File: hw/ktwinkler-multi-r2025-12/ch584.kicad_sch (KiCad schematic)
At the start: 13 parts, among them J10 Conn_01x06, J17 Conn_01x02, J18 Conn_01x02, J3 Conn_01x05, U8 CH584F, Y4 32k, Y5 32M

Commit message: hw: save before kicad 10 upgrade
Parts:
- removed J3: Conn_01x05, Connector_PinHeader_2.54mm:PinHeader_1x05_P2.54mm_Vertical, symbol Connector_Generic:Conn_01x05
- added J19: Conn_01x06, Connector_PinHeader_2.54mm:PinHeader_1x06_P2.54mm_Vertical, symbol Connector_Generic:Conn_01x06
- J10: now left out of the parts list
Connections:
- net GND: now also J19.1 (Pin_1), J19.2 (Pin_2)
- net TCK: now also J19.5 (Pin_5)
- net TIO: now also J19.6 (Pin_6)
- net at U8.27 (PA5_TXD3_AIN1): now also J19.4 (Pin_4)
- net at U8.26 (PA4_RXD3_AIN0): now also J19.3 (Pin_3)
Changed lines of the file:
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@@
 	)
 	(junction
+		(at 198.12 104.14)
+		(diameter 0)
+		(color 0 0 0 0)
+	)
+	(junction
 		(at 106.68 60.96)
 		(diameter 0)
@@
 	(wire
 		(pts
-			(xy 198.12 104.14) (xy 200.66 104.14)
-		)
-		(stroke
-			(width 0)
-			(type default)
-		)
-	)
-	(wire
-		(pts
 			(xy 187.96 114.3) (xy 187.96 109.22)
 		)
@@
 	(wire
 		(pts
+			(xy 200.66 101.6) (xy 198.12 101.6)
+		)
+		(stroke
+			(width 0)
+			(type default)
+		)
+	)
+	(wire
+		(pts
 			(xy 96.52 35.56) (xy 96.52 43.18)
 		)
@@
 	(wire
 		(pts
+			(xy 198.12 101.6) (xy 198.12 104.14)
+		)
+		(stroke
+			(width 0)
+			(type default)
+		)
+	)
+	(wire
+		(pts
 			(xy 119.38 40.64) (xy 119.38 38.1)
 		)
@@
 	(wire
 		(pts
+			(xy 198.12 104.14) (xy 200.66 104.14)
+		)
+		(stroke
+			(width 0)
+			(type default)
+		)
+	)
+	(wire
+		(pts
 			(xy 33.02 101.6) (xy 38.1 101.6)
 		)
@@
 		)
 	)
-	(symbol
-		(lib_id "Connector_Generic:Conn_01x02")
-		(at 83.82 109.22 0)
-		(mirror y)
-		(unit 1)
-		(exclude_from_sim no)
-		(in_bom yes)
-		(on_board yes)
-		(dnp no)
-		(property "Reference" "J17"
-			(at 82.5499 106.68 90)
-			(effects
-				(font
-					(size 1.27 1.27)
-				)
-				(justify left)
+	(netclass_flag ""
+		(length 2.54)
+		(shape round)
+		(at 180.34 38.1 0)
+		(fields_autoplaced yes)
+		(effects
+			(font
+				(size 1.27 1.27)
 			)
+			(justify left bottom)
 		)
-		(property "Value" "Conn_01x02"
-			(at 85.0899 106.68 90)
+		(property "Netclass" "k50r"
+			(at 181.0385 35.56 0)
 			(effects
 				(font
@@
 			)
 		)
-		(property "Footprint" "TestPoint:TestPoint_2Pads_Pitch2.54mm_Drill0.8mm"
-			(at 83.82 109.22 0)
+		(property "Component Class" ""
+			(at -93.98 30.48 0)
 			(effects
 				(font
 					(size 1.27 1.27)
+					(italic yes)
 				)
-				(hide yes)
 			)
 		)
-		(property "Datasheet" "~"
-			(at 83.82 109.22 0)
+	)
+	(netclass_flag ""
+		(length 2.54)
+		(shape round)
+		(at 165.1 38.1 0)
+		(fields_autoplaced yes)
+		(effects
+			(font
+				(size 1.27 1.27)
+			)
+			(justify left bottom)
+		)
+		(property "Netclass" "k50r"
+			(at 165.7985 35.56 0)
 			(effects
 				(font
 					(size 1.27 1.27)
 				)
-				(hide yes)
+				(justify left)
 			)
 		)
-		(property "Description" "Generic connector, single row, 01x02, script generated (kicad-library-utils/schlib/autogen/connector/)"
-			(at 83.82 109.22 0)
+		(property "Component Class" ""
+			(at -109.22 30.48 0)
 			(effects
 				(font
 					(size 1.27 1.27)
-				)
-				(hide yes)
-			)
-		)
-		(pin "2"
-		)
-		(pin "1"
-		)
-		(instances
-			(project "ktwinkler-multi-r2025-12"
-				(path "/48773b41-b773-40e2-8ba4-2e78c7a3e45f/53d46c4f-1818-40ae-8741-bfb04415b511"
-					(reference "J17")
-					(unit 1)
+					(italic yes)
 				)
 			)
@@
 	)
 	(symbol
-		(lib_id "Connector_Generic:Conn_01x05")
-		(at 205.74 109.22 0)
-		(mirror x)
+		(lib_id "Connector_Generic:Conn_01x02")
+		(at 83.82 109.22 0)
+		(mirror y)
 		(unit 1)
 		(exclude_from_sim no)
@@
 		(on_board yes)
 		(dnp no)
-		(fields_autoplaced yes)
-		(property "Reference" "J3"
-			(at 205.74 97.79 0)
+		(property "Reference" "J17"
+			(at 82.5499 106.68 90)
 			(effects
 				(font
 					(size 1.27 1.27)
 				)
+				(justify left)
 			)
 		)
-		(property "Value" "Conn_01x05"
-			(at 205.74 100.33 0)
+		(property "Value" "Conn_01x02"
+			(at 85.0899 106.68 90)
 			(effects
 				(font
 					(size 1.27 1.27)
 				)
+				(justify left)
 			)
 		)
-		(property "Footprint" "Connector_PinHeader_2.54mm:PinHeader_1x05_P2.54mm_Vertical"
-			(at 205.74 109.22 0)
+		(property "Footprint" "TestPoint:TestPoint_2Pads_Pitch2.54mm_Drill0.8mm"
+			(at 83.82 109.22 0)
 			(effects
 				(font
@@
 		)
 		(property "Datasheet" "~"
-			(at 205.74 109.22 0)
+			(at 83.82 109.22 0)
 			(effects
 				(font
@@
 			)
 		)
-		(property "Description" "Generic connector, single row, 01x05, script generated (kicad-library-utils/schlib/autogen/connector/)"
-			(at 205.74 109.22 0)
+		(property "Description" "Generic connector, single row, 01x02, script generated (kicad-library-utils/schlib/autogen/connector/)"
+			(at 83.82 109.22 0)
 			(effects
 				(font
@@
 			)
 		)
-		(pin "1"
-		)
-		(pin "3"
-		)
 		(pin "2"
 		)
-		(pin "4"
-		)
-		(pin "5"
+		(pin "1"
 		)
 		(instances
-			(project ""
+			(project "ktwinkler-multi-r2025-12"
 				(path "/48773b41-b773-40e2-8ba4-2e78c7a3e45f/53d46c4f-1818-40ae-8741-bfb04415b511"
-					(reference "J3")
+					(reference "J17")
 					(unit 1)
 				)
@@
 		(unit 1)
 		(exclude_from_sim no)
-		(in_bom yes)
+		(in_bom no)
 		(on_board yes)
 		(dnp no)
@@
 					(unit 1)
 				)
+			)
+		)
+	)
+	(symbol
+		(lib_id "Connector_Generic:Conn_01x06")
+		(at 205.74 106.68 0)
+		(unit 1)
+		(exclude_from_sim no)
+		(in_bom no)
+		(on_board yes)
+		(dnp no)
+		(property "Reference" "J19"
+			(at 205.74 120.65 0)
+			(effects
+				(font
+					(size 1.27 1.27)
+				)
+			)
+		)
+		(property "Value" "Conn_01x06"
+			(at 205.74 118.11 0)
+			(effects
+				(font
+					(size 1.27 1.27)
+				)
+			)
+		)
+		(property "Footprint" "Connector_PinHeader_2.54mm:PinHeader_1x06_P2.54mm_Vertical"
+			(at 205.74 106.68 0)
+			(effects
+				(font
+					(size 1.27 1.27)
+				)
+				(hide yes)
+			)
+		)
+		(property "Datasheet" "~"
+			(at 205.74 106.68 0)
+			(effects
+				(font
+					(size 1.27 1.27)
+				)
+				(hide yes)
+			)
+		)
+		(property "Description" "Generic connector, single row, 01x06, script generated (kicad-library-utils/schlib/autogen/connector/)"
+			(at 205.74 106.68 0)
+			(effects
+				(font
+					(size 1.27 1.27)
+				)
+				(hide yes)
+			)
+		)
+		(pin "1"
+		)
+		(pin "2"
+		)
+		(pin "3"
+		)
+		(pin "4"
+		)
+		(pin "5"
+		)
+		(pin "6"
+		)
+		(instances
+			(project "ktwinkler-multi-r2025-12"
+				(path "/48773b41-b773-40e2-8ba4-2e78c7a3e45f/53d46c4f-1818-40ae-8741-bfb04415b511"
+					(reference "J19")
+					(unit 1)
+				)

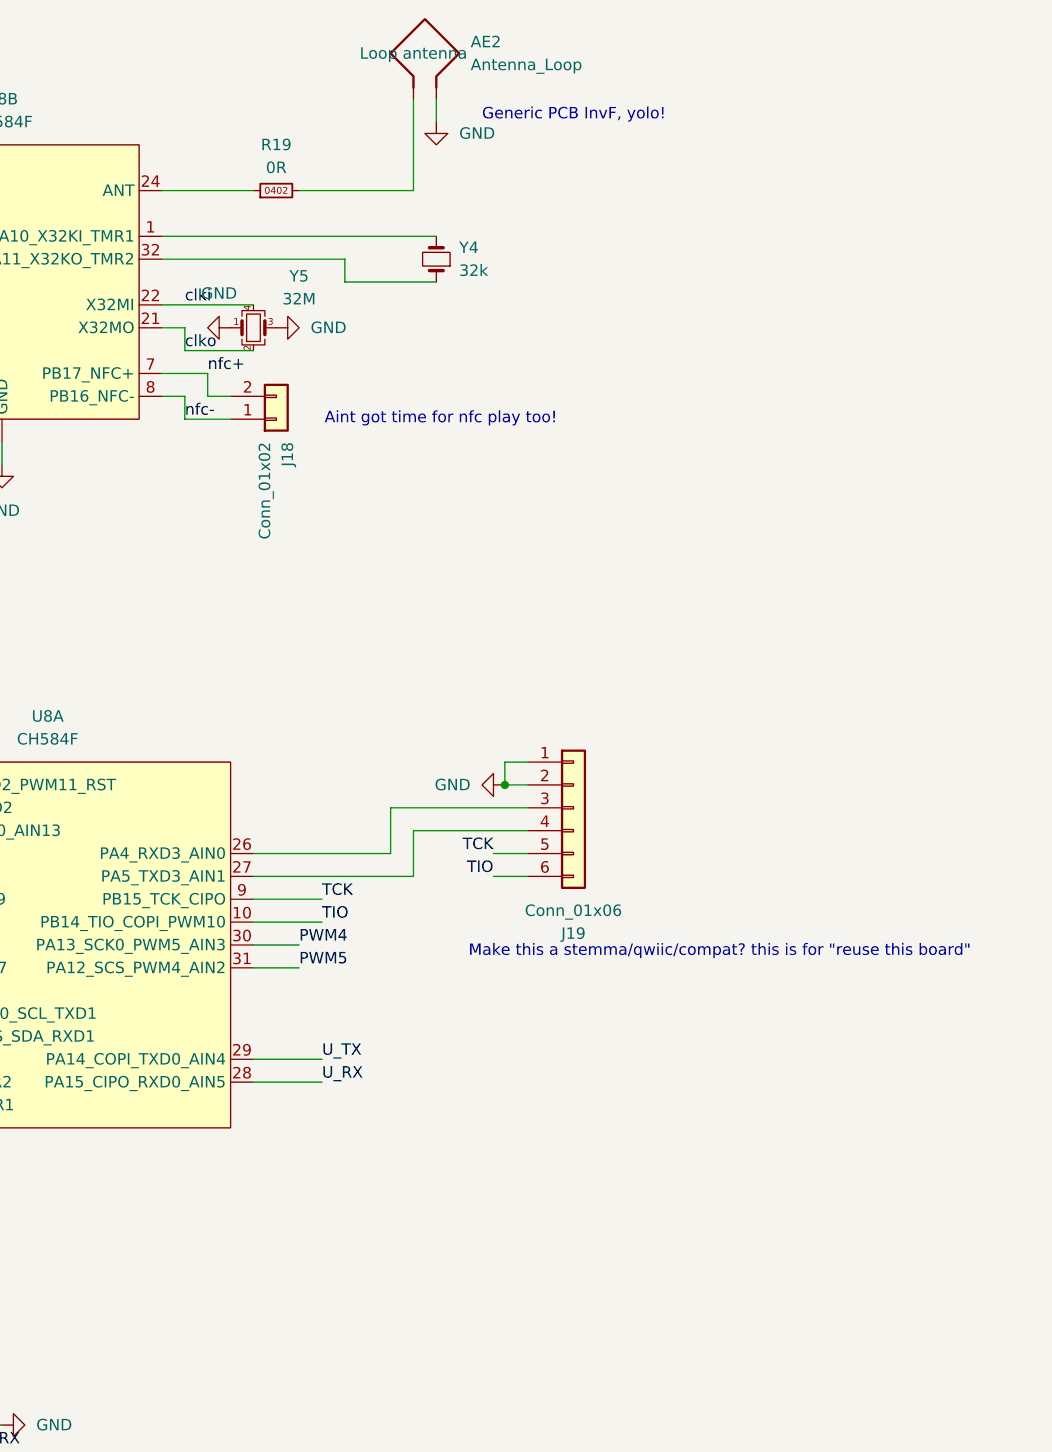
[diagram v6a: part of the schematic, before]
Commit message: hw: update to kicad 10 and order
We added a late qwiic connector to the ch584 side, why not, try that out
too.  We also fixed our smtso footprint, we hope...

Fuck poking the rf more, we're yolo-poling...
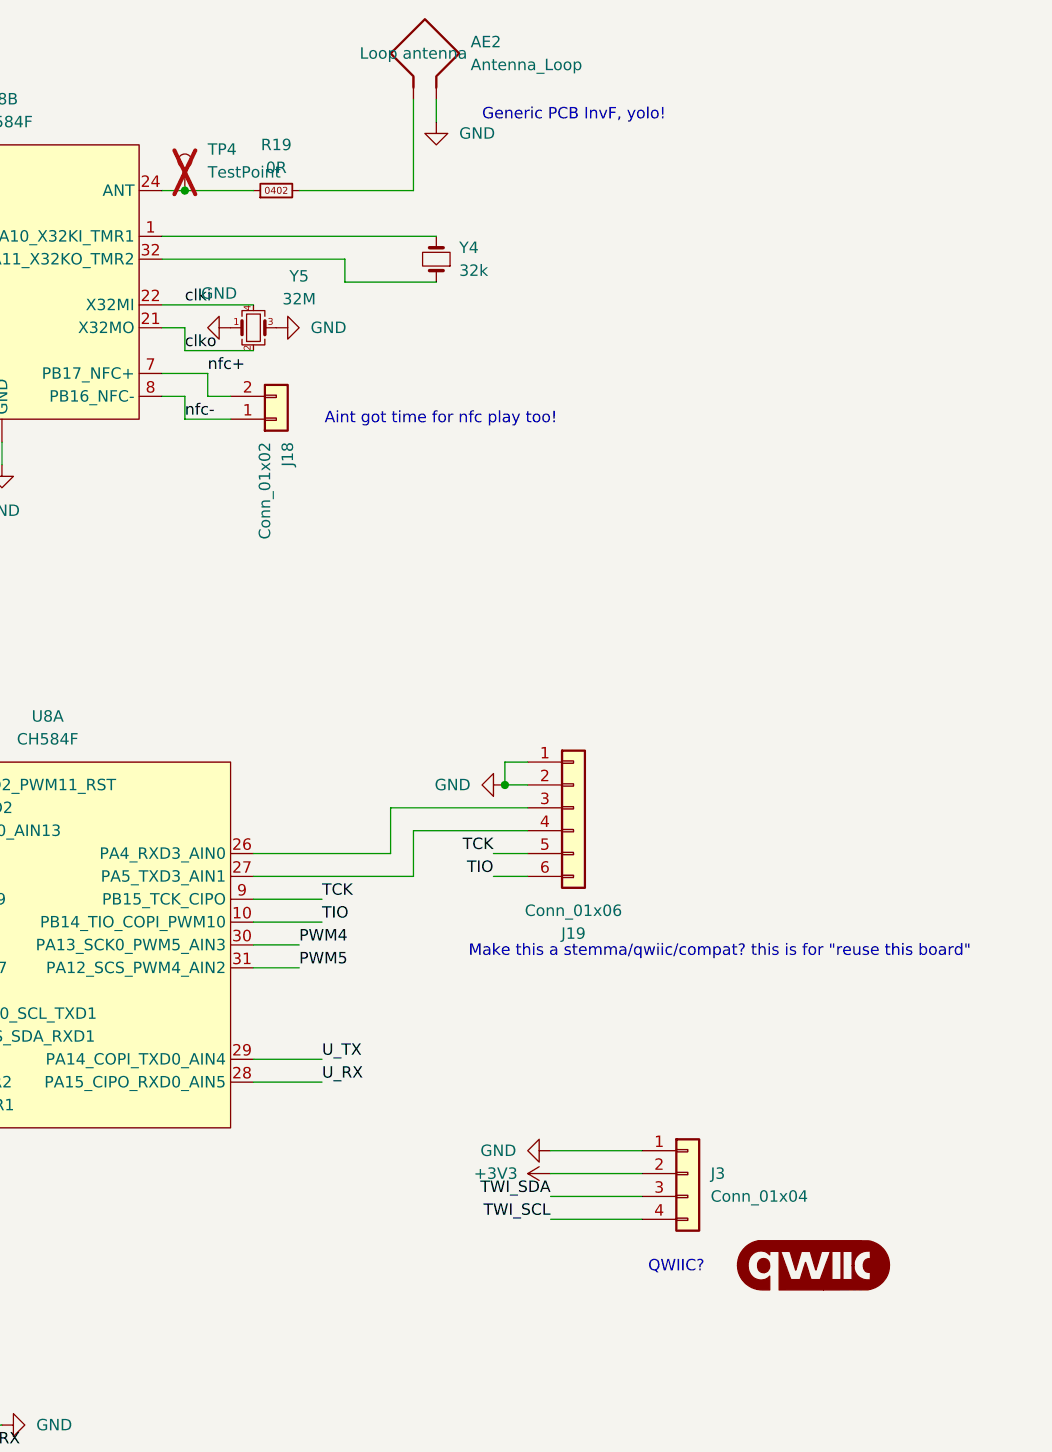
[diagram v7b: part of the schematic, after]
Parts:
- added G1: qwiic_Logo, SparkFun-Qwiic:qwiic_4mm, symbol SparkFun-Qwiic:qwiic_Logo
- added J3: Conn_01x04, Connector_JST:JST_SH_SM04B-SRSS-TB_1x04-1MP_P1.00mm_Horizontal, symbol Connector_Generic:Conn_01x04
- added TP4: TestPoint, TestPoint:TestPoint_Pad_D1.0mm, symbol Connector:TestPoint
- AE2, J17, J18, TP1: now left out of the parts list
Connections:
- net +3V3: now also J3.2 (Pin_2)
- net GND: now also J3.1 (Pin_1)
- net TWI_SCL: now also J3.4 (Pin_4)
- net TWI_SDA: now also J3.3 (Pin_3)
- net at R19.1, U8.24 (ANT): now also TP4.1
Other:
- note added: "QWIIC?"
